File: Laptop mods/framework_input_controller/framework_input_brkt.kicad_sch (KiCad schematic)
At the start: 74 parts

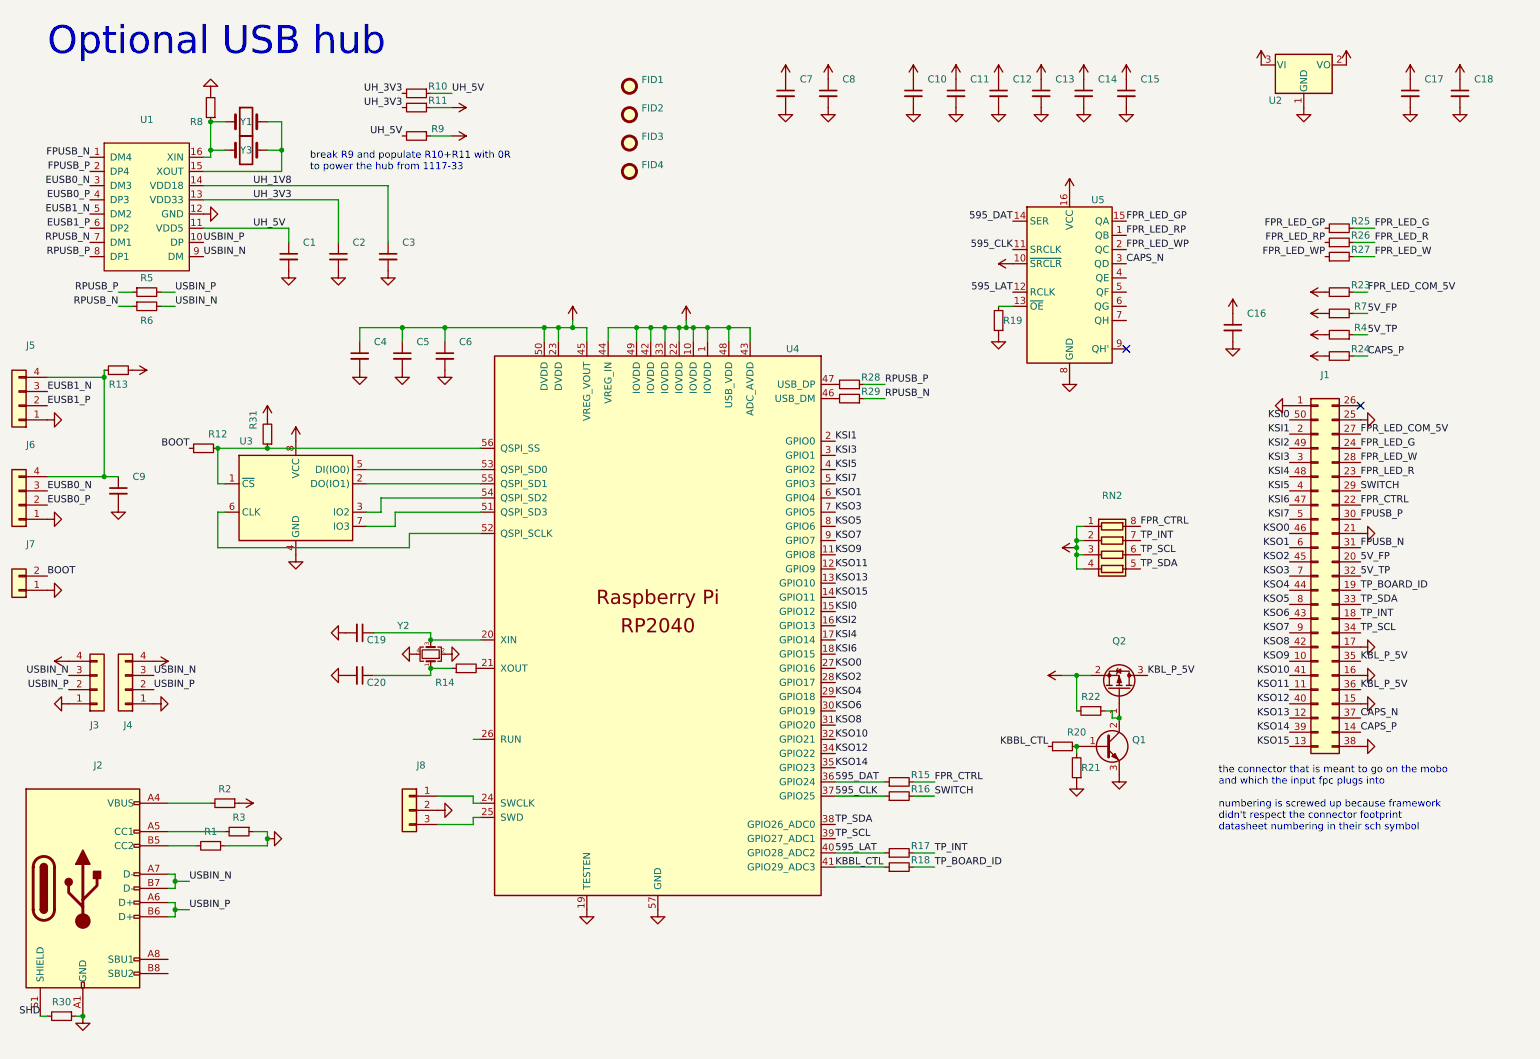
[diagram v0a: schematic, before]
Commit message: framework_input_controller: v2, routing fixes, PCBA optimization, small updates and bugfixes
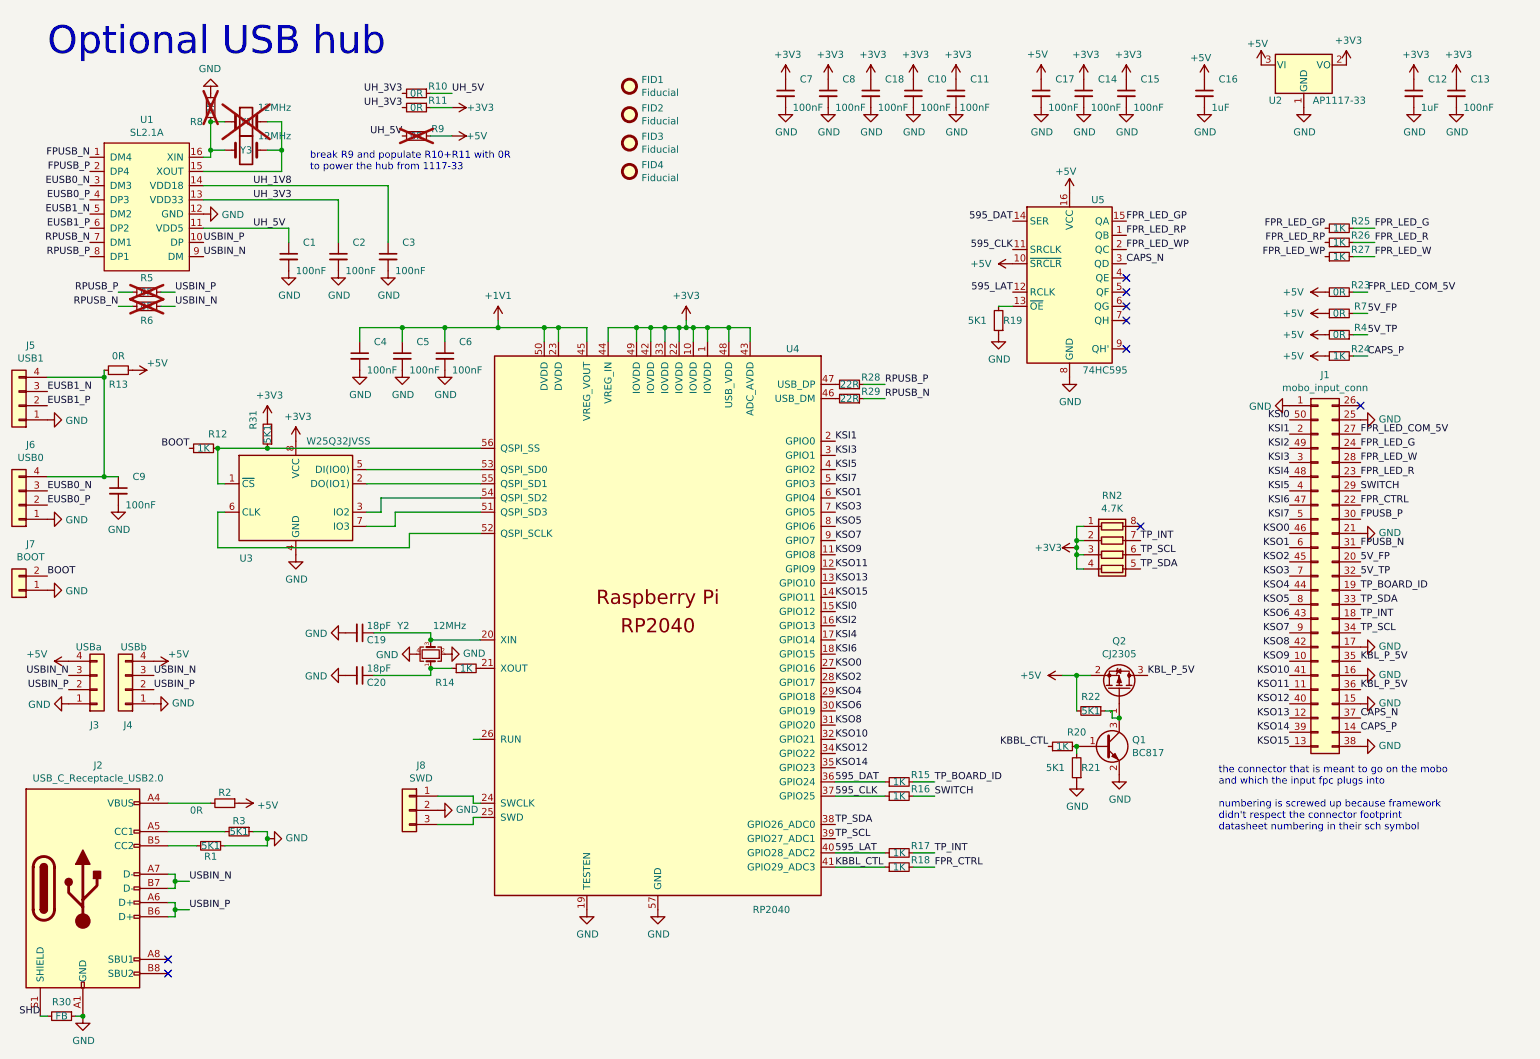
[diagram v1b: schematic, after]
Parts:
- C1, C10, C11, C13, C14, C15, C17, C18, C2, C3, C4, C5, C7, C8, C9: value (none) -> 100nF; footprint (none) -> Capacitor_SMD:C_0603_1608Metric
- C12, C16: value (none) -> 1uF; footprint (none) -> Capacitor_SMD:C_0603_1608Metric
- C19, C20: value (none) -> 18pF; footprint (none) -> Capacitor_SMD:C_0603_1608Metric
- C6: value (none) -> 100nF; footprint (none) -> Resistor_SMD:R_0603_1608Metric
- FID1, FID2, FID3, FID4: value (none) -> Fiducial; footprint (none) -> Fiducial:Fiducial_1mm_Mask2mm
- J1: value (none) -> mobo_input_conn; footprint (none) -> framework_input_brkt:Amphenol_10156000
- J2: value (none) -> USB_C_Receptacle_USB2.0; footprint (none) -> Connector_USB:USB_C_Receptacle_HRO_TYPE-C-31-M-12
- J3: value (none) -> USBa; footprint (none) -> Connector_PinHeader_2.54mm:PinHeader_1x04_P2.54mm_Vertical; now left out of the parts list
- J4: value (none) -> USBb; footprint (none) -> Connector_PinHeader_2.54mm:PinHeader_1x04_P2.54mm_Vertical; now left out of the parts list
- J5: value (none) -> USB1; footprint (none) -> Connector_PinHeader_2.54mm:PinHeader_1x04_P2.54mm_Vertical; now left out of the parts list
- J6: value (none) -> USB0; footprint (none) -> Connector_PinHeader_2.54mm:PinHeader_1x04_P2.54mm_Vertical; now left out of the parts list
- J7: value (none) -> BOOT; footprint (none) -> Connector_PinHeader_2.54mm:PinHeader_1x02_P2.54mm_Vertical; now left out of the parts list
- J8: value (none) -> SWD; footprint (none) -> Connector_PinHeader_2.54mm:PinHeader_1x03_P2.54mm_Vertical; now left out of the parts list
- Q1: value (none) -> BC817; footprint (none) -> Package_TO_SOT_SMD:SOT-23; symbol Device:Q_NPN_BCE -> Device:Q_NPN_BEC
- Q2: value (none) -> CJ2305; footprint (none) -> Package_TO_SOT_SMD:SOT-23
- R1, R19, R21, R22, R3, R31: value (none) -> 5K1; footprint (none) -> Resistor_SMD:R_0603_1608Metric
- R10, R11, R23, R4, R7: value (none) -> 0R; footprint (none) -> Resistor_SMD:R_0603_1608Metric
- R12, R14, R15, R16, R17, R18, R20, R24, R25, R26, R27: value (none) -> 1K; footprint (none) -> Resistor_SMD:R_0603_1608Metric
- R13, R2: value (none) -> 0R; footprint (none) -> Resistor_SMD:R_0805_2012Metric
- R28, R29: value (none) -> 22R; footprint (none) -> Resistor_SMD:R_0402_1005Metric
- R30: value (none) -> FB; footprint (none) -> Resistor_SMD:R_0805_2012Metric
- R5, R6, R8, R9: value (none) -> 0R; footprint (none) -> Resistor_SMD:R_0603_1608Metric; now not fitted; now left out of the parts list
- RN2: value (none) -> 4.7K; footprint (none) -> Resistor_SMD:R_Array_Concave_4x0603
- U1: value (none) -> SL2.1A; footprint (none) -> Package_SO:SO-16_3.9x9.9mm_P1.27mm
- U2: value (none) -> AP1117-33; footprint (none) -> Package_TO_SOT_SMD:SOT-223-3_TabPin2
- U3: value (none) -> W25Q32JVSS; footprint (none) -> Package_SO:SOIC-8_5.23x5.23mm_P1.27mm
- U4: value (none) -> RP2040; footprint (none) -> framework_input_brkt:RP2040-QFN-56
- U5: value (none) -> 74HC595; footprint (none) -> Package_SO:SO-16_3.9x9.9mm_P1.27mm
- Y1: value (none) -> 12MHz; footprint (none) -> Crystal:Crystal_HC49-U_Vertical; now not fitted; now left out of the parts list
- Y2: value (none) -> 12MHz; footprint (none) -> Crystal:Crystal_SMD_3225-4Pin_3.2x2.5mm
- Y3: value (none) -> 12MHz; footprint (none) -> Crystal:Crystal_SMD_HC49-SD
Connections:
- net FPR_CTRL: now also R18.2; no longer R15.2, RN2.8 (R1.2)
- net GND: now also Q1.2 (E); no longer Q1.3 (E)
- net TP_BOARD_ID: now also R15.2; no longer R18.2
- net at Q2.1 (G), R22.1: now also Q1.3 (C); no longer Q1.2 (C)
- no-connect marks 2 -> 9
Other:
- moved on the sheet: C12, C13, C16, C17, C18

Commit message: framework_input_controller: iirc latest version as produced, changes not known
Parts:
- added H1, H2: MountingHole, MountingHole:MountingHole_3mm, symbol Mechanical:MountingHole
- added Y4: 12MHz, Crystal:Crystal_SMD_3225-4Pin_3.2x2.5mm, symbol Device:Crystal_GND24_Small
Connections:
- net GND: now also Y4.2, Y4.4
- net at U1.15 (XOUT), Y1.2, Y3.2: now also Y4.1
- net at R8.1, U1.16 (XIN), Y1.1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: now also Y4.3
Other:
- note added: "the connector that is meant to go on the mobo and which the input fpc plugs into numbering is screwed up because compal didn't respect the connector footprint datasheet numbering in their sch symbol for the framework motherboard"
- note removed: "the connector that is meant to go on the mobo and which the input fpc plugs into numbering is screwed up because framework didn't respect the connector footprint datasheet numbering in their sch symbol"
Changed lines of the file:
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@@
   (junction (at 31.75 76.2) (diameter 0) (color 0 0 0 0)
   )
+  (junction (at 61.595 30.48) (diameter 0) (color 0 0 0 0)
+  )
   (junction (at 132.08 67.31) (diameter 0) (color 0 0 0 0)
   )
@@
   (junction (at 50.8 30.48) (diameter 0) (color 0 0 0 0)
   )
+  (junction (at 52.705 30.48) (diameter 0) (color 0 0 0 0)
+  )
   (junction (at 63.5 35.56) (diameter 0) (color 0 0 0 0)
   )
@@
     (stroke (width 0) (type default))
   )
+  (wire (pts (xy 52.705 30.48) (xy 53.34 30.48))
+    (stroke (width 0) (type default))
+  )
   (wire (pts (xy 205.74 105.41) (xy 205.74 106.68))
     (stroke (width 0) (type default))
@@
     (stroke (width 0) (type default))
   )
+  (wire (pts (xy 61.595 30.48) (xy 60.96 30.48))
+    (stroke (width 0) (type default))
+  )
   (wire (pts (xy 53.34 160.02) (xy 60.96 160.02))
     (stroke (width 0) (type default))
@@
     (stroke (width 0) (type default))
   )
+  (wire (pts (xy 66.675 20.32) (xy 52.705 20.32))
+    (stroke (width 0) (type default))
+  )
   (wire (pts (xy 90.17 25.4) (xy 93.98 25.4))
     (stroke (width 0) (type default))
@@
     (stroke (width 0) (type default))
   )
+  (wire (pts (xy 61.595 25.4) (xy 61.595 30.48))
+    (stroke (width 0) (type default))
+  )
   (wire (pts (xy 180.34 151.13) (xy 176.53 151.13))
     (stroke (width 0) (type default))
@@
     (stroke (width 0) (type default))
   )
-  (wire (pts (xy 63.5 30.48) (xy 60.96 30.48))
+  (wire (pts (xy 63.5 30.48) (xy 61.595 30.48))
     (stroke (width 0) (type default))
   )
@@
     (stroke (width 0) (type default))
   )
+  (wire (pts (xy 52.705 20.32) (xy 52.705 30.48))
+    (stroke (width 0) (type default))
+  )
   (wire (pts (xy 167.64 80.01) (xy 171.45 80.01))
     (stroke (width 0) (type default))
@@
     (stroke (width 0) (type default))
   )
-  (wire (pts (xy 50.8 30.48) (xy 53.34 30.48))
+  (wire (pts (xy 50.8 30.48) (xy 52.705 30.48))
     (stroke (width 0) (type default))
   )
@@
     (stroke (width 0) (type default))
   )
+  (wire (pts (xy 66.675 25.4) (xy 61.595 25.4))
+    (stroke (width 0) (type default))
+  )
   (wire (pts (xy 44.45 166.37) (xy 44.45 165.1))
     (stroke (width 0) (type default))
@@
     (effects (font (size 5.0038 5.0038)) (justify left bottom))
   )
-  (text "the connector that is meant to go on the mobo\nand which the input fpc plugs into\n\nnumbering is screwed up because framework\ndidn't respect the connector footprint\ndatasheet numbering in their sch symbol"
-    (at 231.14 157.48 0)
+  (text "the connector that is meant to go on the mobo\nand which the input fpc plugs into\n\nnumbering is screwed up because compal\ndidn't respect the connector footprint\ndatasheet numbering in their sch symbol\nfor the framework motherboard"
+    (at 230.505 161.29 0)
     (effects (font (size 1.27 1.27)) (justify left bottom))
   )
@@
         )
       )
+    )
+  )
+  (symbol (lib_id "power:GND") (at 69.215 22.86 90) (unit 1)
+    (in_bom yes) (on_board yes) (dnp no)
+    (property "Reference" "#PWR019" (at 75.565 22.86 0)
+      (effects (font (size 1.27 1.27)) hide)
+    )
+    (property "Value" "GND" (at 72.4662 22.733 90)
+      (effects (font (size 1.27 1.27)) (justify right))
+    )
+    (property "Footprint" "" (at 69.215 22.86 0)
+      (effects (font (size 1.27 1.27)) hide)
+    )
+    (property "Datasheet" "" (at 69.215 22.86 0)
+      (effects (font (size 1.27 1.27)) hide)
+    )
+    (pin "1")
+    (instances
+      (project "framework_input_brkt"
+        (path "/3e001963-6eae-4c22-8e3f-a4653318a66f"
+          (reference "#PWR019") (unit 1)
+        )
+      )
+    )
+  )
+  (symbol (lib_id "Device:Crystal_GND24_Small") (at 66.675 22.86 90) (unit 1)
+    (in_bom yes) (on_board yes) (dnp no)
+    (property "Reference" "Y4" (at 62.865 17.78 90)
+      (effects (font (size 1.27 1.27)) (justify left))
+    )
+    (property "Value" "12MHz" (at 73.66 20.32 90)
+      (effects (font (size 1.27 1.27)) (justify left))
+    )
+    (property "Footprint" "Crystal:Crystal_SMD_3225-4Pin_3.2x2.5mm" (at 66.675 22.86 0)
+      (effects (font (size 1.27 1.27)) hide)
+    )
+    (property "Datasheet" "~" (at 66.675 22.86 0)
+      (effects (font (size 1.27 1.27)) hide)
+    )
+    (pin "1")
+    (pin "2")
+    (pin "3")
+    (pin "4")
+    (instances
+      (project "framework_input_brkt"
+        (path "/3e001963-6eae-4c22-8e3f-a4653318a66f"
+          (reference "Y4") (unit 1)
+        )
+      )
+    )
+  )
+  (symbol (lib_id "power:GND") (at 64.135 22.86 270) (unit 1)
+    (in_bom yes) (on_board yes) (dnp no)
+    (property "Reference" "#PWR016" (at 57.785 22.86 0)
+      (effects (font (size 1.27 1.27)) hide)
+    )
+    (property "Value" "GND" (at 60.8838 22.987 90)
+      (effects (font (size 1.27 1.27)) (justify right))
+    )
+    (property "Footprint" "" (at 64.135 22.86 0)
+      (effects (font (size 1.27 1.27)) hide)
+    )
+    (property "Datasheet" "" (at 64.135 22.86 0)
+      (effects (font (size 1.27 1.27)) hide)
+    )
+    (pin "1")
+    (instances
+      (project "framework_input_brkt"
+        (path "/3e001963-6eae-4c22-8e3f-a4653318a66f"
+          (reference "#PWR016") (unit 1)
+        )
+      )
+    )
+  )
+  (symbol (lib_id "Mechanical:MountingHole") (at 75.565 177.8 0) (unit 1)
+    (in_bom yes) (on_board yes) (dnp no) (fields_autoplaced)
+    (property "Reference" "H1" (at 78.105 176.5879 0)
+      (effects (font (size 1.27 1.27)) (justify left))
+    )
+    (property "Value" "MountingHole" (at 78.105 179.0121 0)
+      (effects (font (size 1.27 1.27)) (justify left))
+    )
+    (property "Footprint" "MountingHole:MountingHole_3mm" (at 75.565 177.8 0)
+      (effects (font (size 1.27 1.27)) hide)
+    )
+    (property "Datasheet" "~" (at 75.565 177.8 0)
+      (effects (font (size 1.27 1.27)) hide)
+    )
+    (instances
+      (project "framework_input_brkt"
+        (path "/3e001963-6eae-4c22-8e3f-a4653318a66f"
+          (reference "H1") (unit 1)
+        )
+      )
+    )
+  )
+  (symbol (lib_id "Mechanical:MountingHole") (at 75.565 182.88 0) (unit 1)
+    (in_bom yes) (on_board yes) (dnp no) (fields_autoplaced)
+    (property "Reference" "H2" (at 78.105 181.6679 0)
+      (effects (font (size 1.27 1.27)) (justify left))
+    )
+    (property "Value" "MountingHole" (at 78.105 184.0921 0)
+      (effects (font (size 1.27 1.27)) (justify left))
+    )
+    (property "Footprint" "MountingHole:MountingHole_3mm" (at 75.565 182.88 0)
+      (effects (font (size 1.27 1.27)) hide)
+    )
+    (property "Datasheet" "~" (at 75.565 182.88 0)
+      (effects (font (size 1.27 1.27)) hide)
+    )
+    (instances
+      (project "framework_input_brkt"
+        (path "/3e001963-6eae-4c22-8e3f-a4653318a66f"
+          (reference "H2") (unit 1)
+        )
+      )
